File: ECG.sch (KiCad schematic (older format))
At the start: 41 parts, among them J1 SJ-3566AN, J2 Conn_01x03, U1 ADR4525, U2 LTC3531, U7 ADS1015IDGS

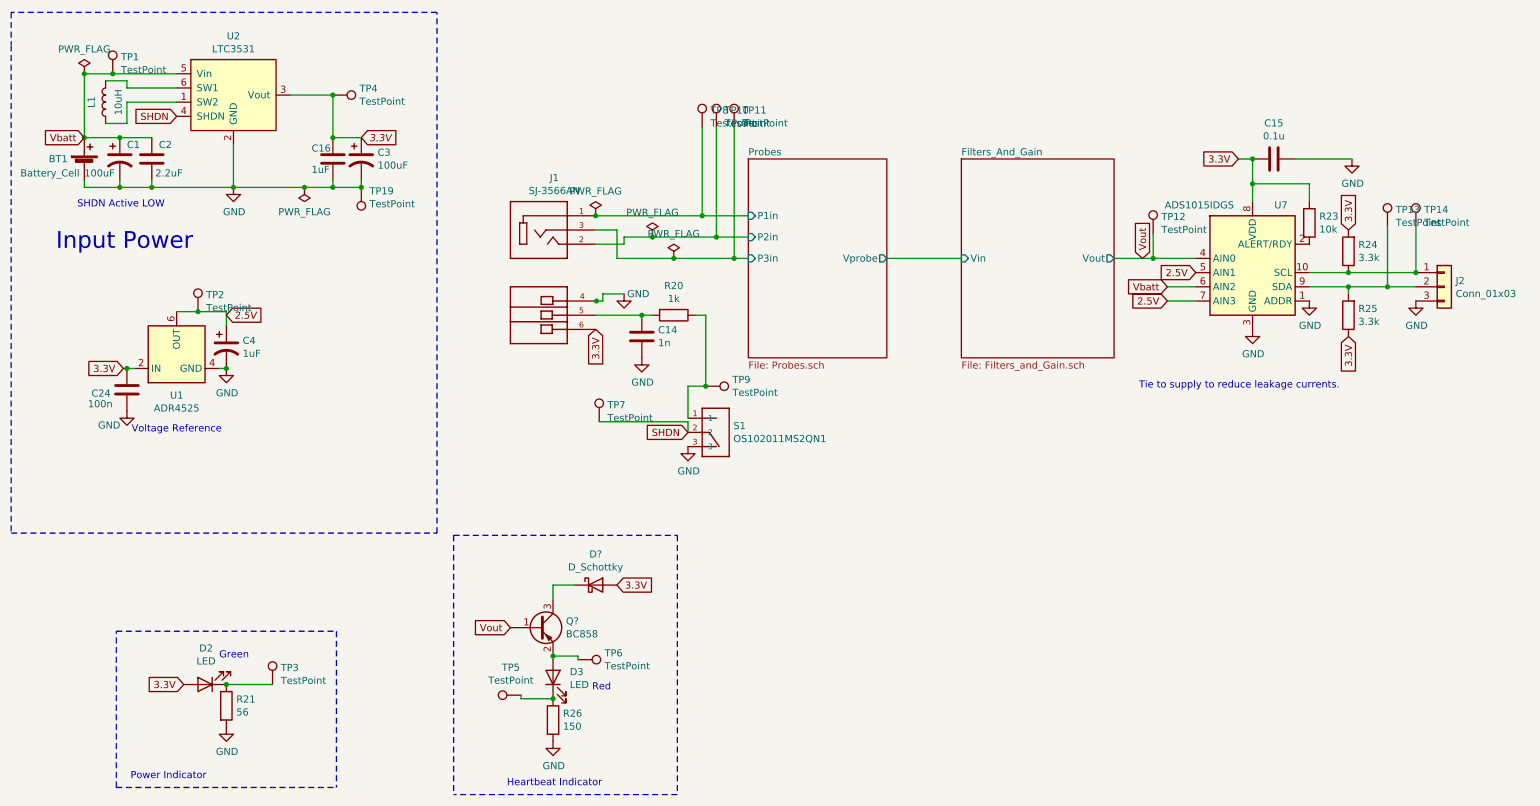
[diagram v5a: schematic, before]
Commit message: #6 - Add bluetooth module to board.
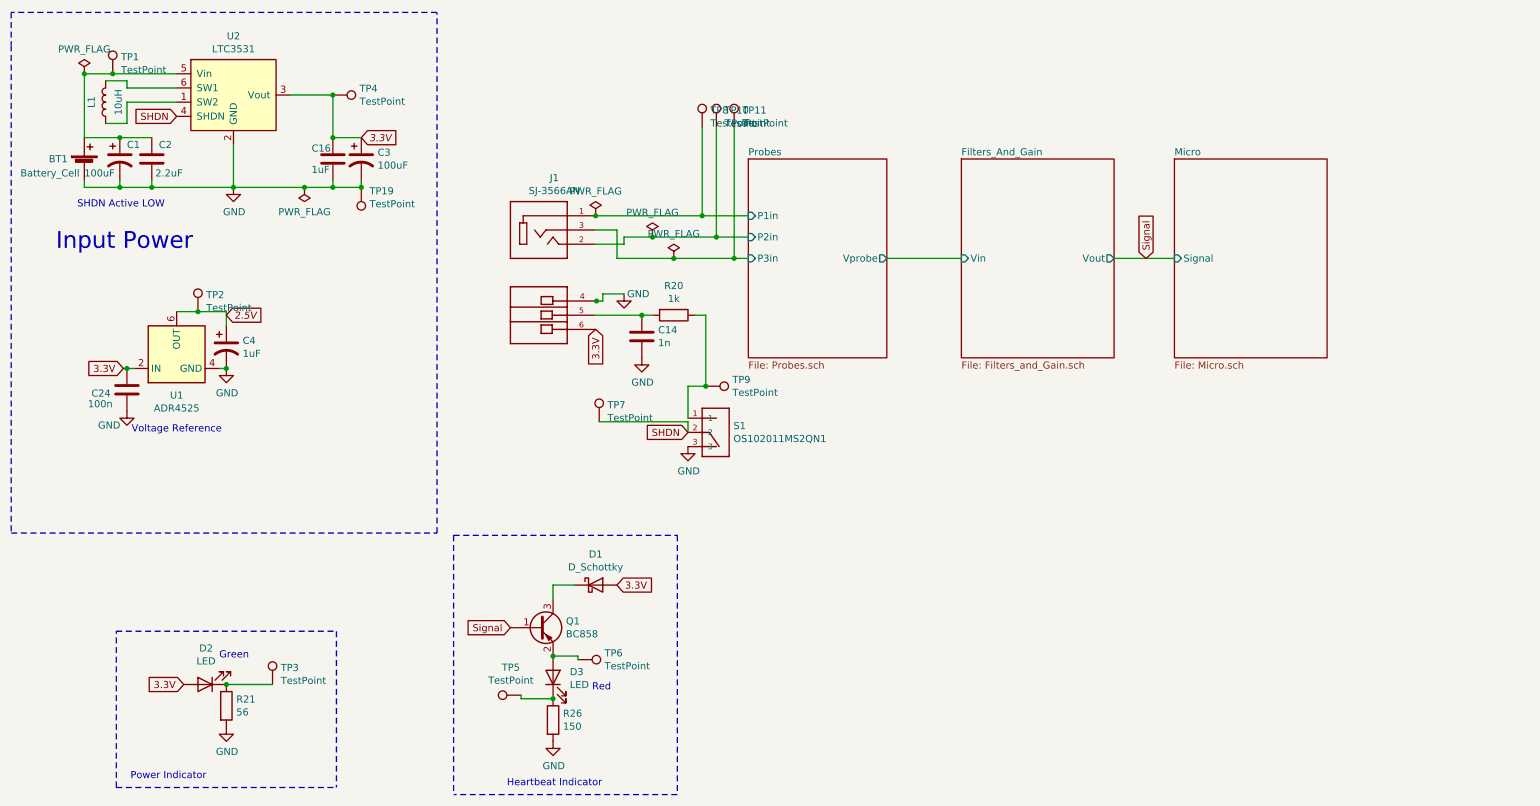
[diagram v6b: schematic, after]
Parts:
- removed C15: 0.1u, Capacitor_SMD:C_0805_2012Metric_Pad1.18x1.45mm_HandSolder, symbol Device:C
- removed J2: Conn_01x03, Connector_PinHeader_2.00mm:PinHeader_1x03_P2.00mm_Vertical, symbol Connector_Generic:Conn_01x03
- removed R23: 10k, Resistor_SMD:R_0805_2012Metric_Pad1.20x1.40mm_HandSolder, symbol Device:R
- removed R24, R25: 3.3k, Resistor_SMD:R_0805_2012Metric_Pad1.20x1.40mm_HandSolder, symbol Device:R
- removed TP12, TP13, TP14: TestPoint, TestPoint:TestPoint_Pad_D2.0mm, symbol Connector:TestPoint
- removed U7: ADS1015IDGS, Package_SO:TSSOP-10_3x3mm_P0.5mm, symbol Analog_ADC:ADS1015IDGS
- gave numbers to parts that had none: 2
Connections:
- net Vbatt: no longer names the net of BT1.1 (+), C1.1, C2.1, TP1.1, U2.5 (Vin)
- net Vout renamed Signal
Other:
- note removed: "Tie to supply to reduce leakage currents."
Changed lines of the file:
@@
 $Descr A4 11693 8268
 encoding utf-8
-Sheet 1 3
+Sheet 1 4
 Title "Power"
 Date ""
@@
 Text Notes 1725 7175 0    50   ~ 0
 Power Indicator
-$Comp
-L Analog_ADC:ADS1015IDGS U7
-U 1 1 5FBE58F1
-P 9625 3600
-F 0 "U7" H 9825 4075 50  0000 C CNN
-F 1 "ADS1015IDGS" H 9250 4075 50  0000 C CNN
-F 2 "Package_SO:TSSOP-10_3x3mm_P0.5mm" H 9625 3100 50  0001 C CNN
-F 3 "http://www.ti.com/lit/ds/symlink/ads1015.pdf" H 9575 2700 50  0001 C CNN
-	1    9625 3600
-	1    0    0    -1
-$EndComp
-$Comp
-L power:GND #PWR015
-U 1 1 5FBF14F2
-P 9625 4000
-F 0 "#PWR015" H 9625 3750 50  0001 C CNN
-F 1 "GND" H 9630 3827 50  0000 C CNN
-F 2 "" H 9625 4000 50  0001 C CNN
-F 3 "" H 9625 4000 50  0001 C CNN
-	1    9625 4000
-	1    0    0    -1
-$EndComp
-Text GLabel 9525 2800 0    50   Input ~ 0
-3.3V
-$Comp
-L Device:C C15
-U 1 1 5FBF2959
-P 9775 2800
-F 0 "C15" V 9523 2800 50  0000 C CNN
-F 1 "0.1u" V 9614 2800 50  0000 C CNN
-F 2 "Capacitor_SMD:C_0805_2012Metric_Pad1.18x1.45mm_HandSolder" H 9813 2650 50  0001 C CNN
-F 3 "~" H 9775 2800 50  0001 C CNN
-	1    9775 2800
-	0    1    1    0
-$EndComp
-Wire Wire Line
-	9625 2800 9625 2975
-Wire Wire Line
-	9625 2800 9525 2800
-Connection ~ 9625 2800
-$Comp
-L power:GND #PWR017
-U 1 1 5FBFA432
-P 10325 2800
-F 0 "#PWR017" H 10325 2550 50  0001 C CNN
-F 1 "GND" H 10330 2627 50  0000 C CNN
-F 2 "" H 10325 2800 50  0001 C CNN
-F 3 "" H 10325 2800 50  0001 C CNN
-	1    10325 2800
-	1    0    0    -1
-$EndComp
-$Comp
-L Device:R R23
-U 1 1 5FC01BDB
-P 10025 3250
-F 0 "R23" H 10095 3296 50  0000 L CNN
-F 1 "10k" H 10095 3205 50  0000 L CNN
-F 2 "Resistor_SMD:R_0805_2012Metric_Pad1.20x1.40mm_HandSolder" V 9955 3250 50  0001 C CNN
-F 3 "~" H 10025 3250 50  0001 C CNN
-	1    10025 3250
-	1    0    0    -1
-$EndComp
-$Comp
-L Device:R R25
-U 1 1 5FC054BC
-P 10300 3900
-F 0 "R25" H 10230 3854 50  0000 R CNN
-F 1 "3.3k" H 10230 3945 50  0000 R CNN
-F 2 "Resistor_SMD:R_0805_2012Metric_Pad1.20x1.40mm_HandSolder" V 10230 3900 50  0001 C CNN
-F 3 "~" H 10300 3900 50  0001 C CNN
-	1    10300 3900
-	-1   0    0    1
-$EndComp
-$Comp
-L Device:R R24
-U 1 1 5FC0648F
-P 10300 3450
-F 0 "R24" H 10230 3404 50  0000 R CNN
-F 1 "3.3k" H 10230 3495 50  0000 R CNN
-F 2 "Resistor_SMD:R_0805_2012Metric_Pad1.20x1.40mm_HandSolder" V 10230 3450 50  0001 C CNN
-F 3 "~" H 10300 3450 50  0001 C CNN
-	1    10300 3450
-	-1   0    0    1
-$EndComp
-Wire Wire Line
-	10025 3700 10300 3700
-Wire Wire Line
-	10300 3700 10300 3750
-Wire Wire Line
-	10300 3700 10575 3700
-Connection ~ 10300 3700
-Wire Wire Line
-	10300 3600 10025 3600
-Connection ~ 10300 3600
-Text GLabel 10300 3300 1    50   Input ~ 0
-3.3V
-Text GLabel 10300 4050 3    50   Input ~ 0
-3.3V
-$Comp
-L power:GND #PWR016
-U 1 1 5FC0ADCB
-P 10025 3800
-F 0 "#PWR016" H 10025 3550 50  0001 C CNN
-F 1 "GND" H 10030 3627 50  0000 C CNN
-F 2 "" H 10025 3800 50  0001 C CNN
-F 3 "" H 10025 3800 50  0001 C CNN
-	1    10025 3800
-	1    0    0    -1
-$EndComp
-Wire Wire Line
-	8650 3500 8925 3500
-Text GLabel 9225 3600 0    50   Input ~ 0
-2.5V
-Wire Wire Line
-	9225 3700 9025 3700
-Wire Wire Line
-	9225 3800 9025 3800
-Text Notes 8825 4425 0    50   ~ 0
-Tie to supply to reduce leakage currents.
-Wire Wire Line
-	9925 2800 10325 2800
-Wire Wire Line
-	10025 3100 10025 2975
-Wire Wire Line
-	10025 2975 9625 2975
-Connection ~ 9625 2975
-Wire Wire Line
-	9625 2975 9625 3100
 Wire Wire Line
 	7050 3500 7575 3500
 Text Notes 2350 6325 0    50   ~ 0
 Green\n
-Text GLabel 8850 3500 1    50   Input ~ 0
-Vout
-Text GLabel 4400 6100 0    50   Input ~ 0
-Vout
 Text GLabel 5150 5800 2    50   Input ~ 0
 3.3V
@@
 Wire Wire Line
 	5650 4725 5650 4650
-$Comp
-L Connector:TestPoint TP14
-U 1 1 5FC95E35
-P 10775 3275
-F 0 "TP14" H 10833 3393 50  0000 L CNN
-F 1 "TestPoint" H 10833 3302 50  0000 L CNN
-F 2 "TestPoint:TestPoint_Pad_D2.0mm" H 10975 3275 50  0001 C CNN
-F 3 "~" H 10975 3275 50  0001 C CNN
-	1    10775 3275
-	1    0    0    -1
-$EndComp
-$Comp
-L Connector:TestPoint TP13
-U 1 1 5FC9653A
-P 10575 3275
-F 0 "TP13" H 10633 3393 50  0000 L CNN
-F 1 "TestPoint" H 10633 3302 50  0000 L CNN
-F 2 "TestPoint:TestPoint_Pad_D2.0mm" H 10775 3275 50  0001 C CNN
-F 3 "~" H 10775 3275 50  0001 C CNN
-	1    10575 3275
-	1    0    0    -1
-$EndComp
-Wire Wire Line
-	10775 3275 10775 3600
-$Comp
-L Connector:TestPoint TP12
-U 1 1 5FCA6AF9
-P 8925 3325
-F 0 "TP12" H 8983 3443 50  0000 L CNN
-F 1 "TestPoint" H 8983 3352 50  0000 L CNN
-F 2 "TestPoint:TestPoint_Pad_D2.0mm" H 9125 3325 50  0001 C CNN
-F 3 "~" H 9125 3325 50  0001 C CNN
-	1    8925 3325
-	1    0    0    -1
-$EndComp
-Wire Wire Line
-	8925 3325 8925 3500
-Connection ~ 8925 3500
-Wire Wire Line
-	8925 3500 9225 3500
 Wire Wire Line
 	4700 6300 4875 6300
@@
 	1    0    0    -1
 $EndComp
-Text GLabel 9025 3700 0    50   Input ~ 0
-Vbatt
-Text GLabel 9025 3800 0    50   Input ~ 0
-2.5V
 Text GLabel 2100 6500 0    50   Input ~ 0
 3.3V
-$Comp
-L Connector_Generic:Conn_01x03 J2
-U 1 1 5FCF854F
-P 10975 3700
-F 0 "J2" H 11055 3742 50  0000 L CNN
-F 1 "Conn_01x03" H 11055 3651 50  0000 L CNN
-F 2 "Connector_PinHeader_2.00mm:PinHeader_1x03_P2.00mm_Vertical" H 10975 3700 50  0001 C CNN
-F 3 "~" H 10975 3700 50  0001 C CNN
-	1    10975 3700
-	1    0    0    -1
-$EndComp
-Connection ~ 10775 3600
-$Comp
-L power:GND #PWR020
-U 1 1 5FCF90A6
-P 10775 3800
-F 0 "#PWR020" H 10775 3550 50  0001 C CNN
-F 1 "GND" H 10780 3627 50  0000 C CNN
-F 2 "" H 10775 3800 50  0001 C CNN
-F 3 "" H 10775 3800 50  0001 C CNN
-	1    10775 3800
-	1    0    0    -1
-$EndComp
 Wire Wire Line
 	6075 3200 5750 3200
@@
 	6075 3500 5975 3500
 Connection ~ 5975 3500
-Connection ~ 10575 3700
-Wire Wire Line
-	10575 3700 10775 3700
-Wire Wire Line
-	10300 3600 10775 3600
-Wire Wire Line
-	10575 3275 10575 3700
 $Comp
 L Device:C C2
@@
 Wire Wire Line
 	1400 2200 1600 2200
-Connection ~ 1400 2650
 Wire Wire Line
 	2050 2400 1700 2400
@@
 Connection ~ 3150 2650
 Connection ~ 3150 2350
-Text GLabel 1400 2650 0    50   Input ~ 0
-Vbatt
 Wire Notes Line
 	1625 6125 3175 6125
@@
 	1625 7225 3175 7225
 $Comp
-L Transistor_BJT:BC858 Q?
+L Transistor_BJT:BC858 Q1
 U 1 1 5FDAC112
 P 4600 6100
-F 0 "Q?" H 4791 6146 50  0000 L CNN
+F 0 "Q1" H 4791 6146 50  0000 L CNN
 F 1 "BC858" H 4791 6055 50  0000 L CNN
 F 2 "Package_TO_SOT_SMD:SOT-23" H 4800 6025 50  0001 L CIN
@@
 	5575 5450 5575 7275
 $Comp
-L Device:D_Schottky D?
+L Device:D_Schottky D1
 U 1 1 5FDC078D
 P 5000 5800
-F 0 "D?" H 5000 6017 50  0000 C CNN
+F 0 "D1" H 5000 6017 50  0000 C CNN
 F 1 "D_Schottky" H 5000 5926 50  0000 C CNN
 F 2 "Diode_SMD:D_0603_1608Metric_Pad1.05x0.95mm_HandSolder" H 5000 5800 50  0001 C CNN
@@
 F3 "Vin" I L 7575 3500 50
 $EndSheet
+$Sheet
+S 9075 2800 1075 1400
+U 5FDD9C20
+F0 "Micro" 50
+F1 "Micro.sch" 50
+F2 "Signal" I L 9075 3500 50
+$EndSheet
+Wire Wire Line
+	9075 3500 8650 3500
+Text GLabel 8875 3500 1    50   Input ~ 0
+Signal
+Text GLabel 4400 6100 0    50   Input ~ 0
+Signal
 $EndSCHEMATC

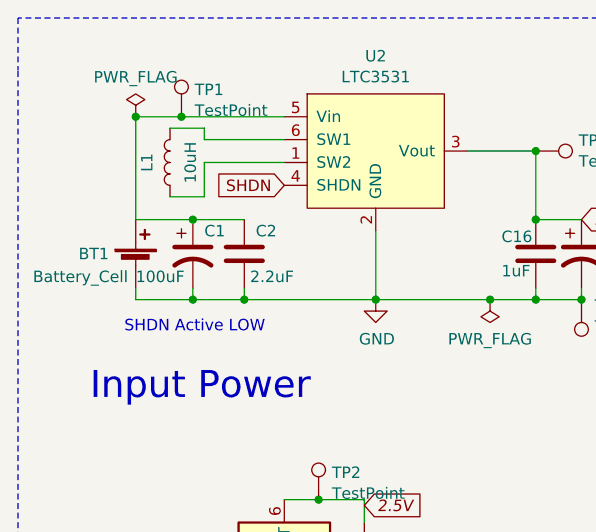
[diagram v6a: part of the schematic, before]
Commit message: #6 #14 - Add bluetooth and flash header to board
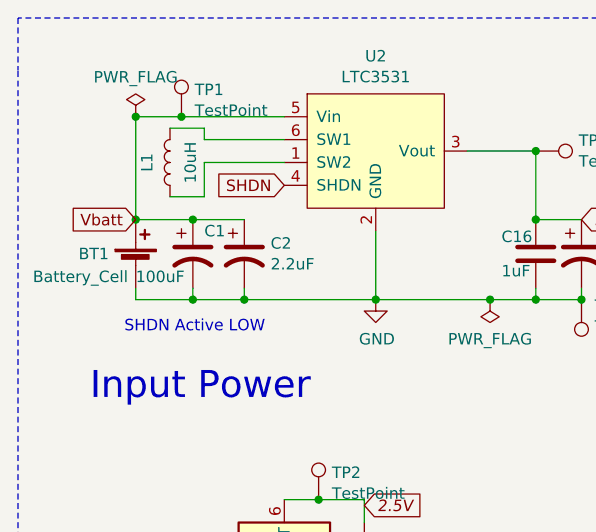
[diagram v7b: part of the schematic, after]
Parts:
- removed C2: 2.2uF, symbol Device:C
- added C2: 2.2uF, Capacitor_SMD:CP_Elec_4x5.7, symbol Device:CP1
- C16: footprint (none) -> Capacitor_SMD:CP_Elec_4x5.3
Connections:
- net GND: now also C2.2
- net Vbatt: now reaches BT1.1 (+), C1.1, TP1.1, U2.5 (Vin)
- net Vbatt: now also C2.1
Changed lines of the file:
@@
 	6075 3500 5975 3500
 Connection ~ 5975 3500
-$Comp
-L Device:C C2
-U 1 1 5FD5C986
-P 1875 2800
-F 0 "C2" H 1925 2900 50  0000 L CNN
-F 1 "2.2uF" H 1900 2700 50  0000 L CNN
-F 2 "" H 1913 2650 50  0001 C CNN
-F 3 "~" H 1875 2800 50  0001 C CNN
-	1    1875 2800
-	1    0    0    -1
-$EndComp
 Connection ~ 1650 2650
 Wire Wire Line
@@
 F 0 "C16" H 3000 2875 50  0000 L CNN
 F 1 "1uF" H 3000 2725 50  0000 L CNN
-F 2 "" H 3188 2650 50  0001 C CNN
+F 2 "Capacitor_SMD:CP_Elec_4x5.3" H 3188 2650 50  0001 C CNN
 F 3 "~" H 3150 2800 50  0001 C CNN
 	1    3150 2800
@@
 Text GLabel 4400 6100 0    50   Input ~ 0
 Signal
+Text GLabel 1400 2650 0    50   Input ~ 0
+Vbatt
+Connection ~ 1400 2650
+$Comp
+L Device:CP1 C2
+U 1 1 5FE0A857
+P 1875 2800
+F 0 "C2" H 1990 2846 50  0000 L CNN
+F 1 "2.2uF" H 1990 2755 50  0000 L CNN
+F 2 "Capacitor_SMD:CP_Elec_4x5.7" H 1875 2800 50  0001 C CNN
+F 3 "~" H 1875 2800 50  0001 C CNN
+	1    1875 2800
+	1    0    0    -1
+$EndComp
 $EndSCHEMATC

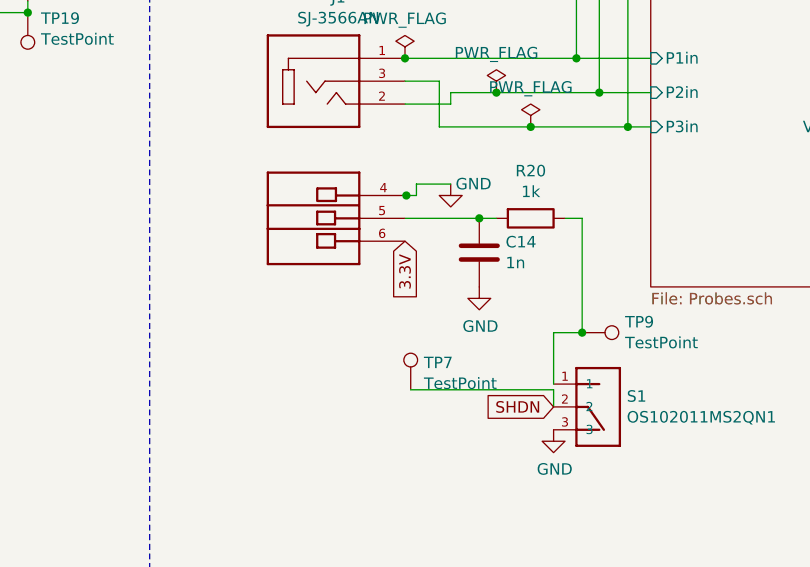
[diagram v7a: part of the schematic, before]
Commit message: #21 - Hook up switch to battery line
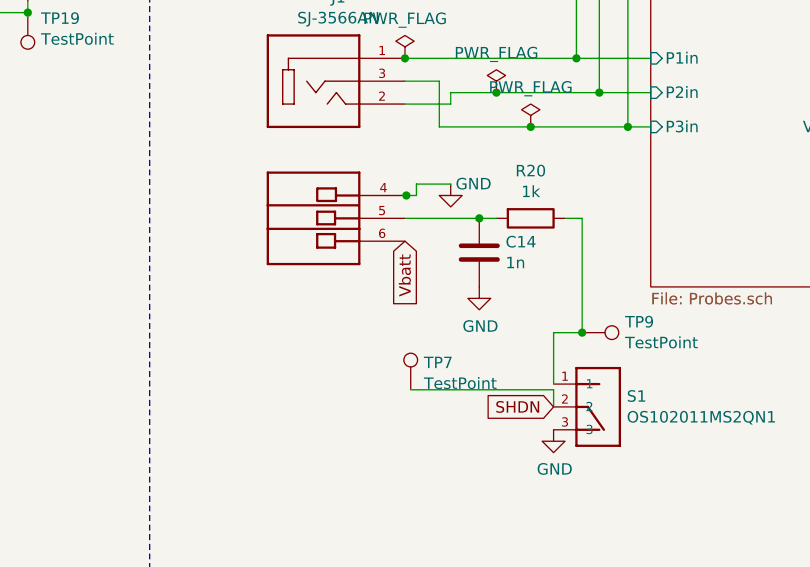
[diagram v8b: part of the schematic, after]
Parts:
- C3: footprint Capacitor_SMD:CP_Elec_5x5.3 -> Capacitor_SMD:CP_Elec_6.3x5.3
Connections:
- net 3.3V: no longer J1.6
- net Vbatt: now also J1.6
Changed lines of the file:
@@
 F 0 "C3" H 3465 2846 50  0000 L CNN
 F 1 "100uF" H 3465 2755 50  0000 L CNN
-F 2 "Capacitor_SMD:CP_Elec_5x5.3" H 3350 2800 50  0001 C CNN
+F 2 "Capacitor_SMD:CP_Elec_6.3x5.3" H 3350 2800 50  0001 C CNN
 F 3 "~" H 3350 2800 50  0001 C CNN
 	1    3350 2800
@@
 	1    0    0    -1
 $EndComp
-Text GLabel 5000 4000 3    50   Input ~ 0
-3.3V
 Wire Wire Line
 	1400 2650 1650 2650
@@
 	1    0    0    -1
 $EndComp
+Text GLabel 5000 4000 3    50   Input ~ 0
+Vbatt
 $EndSCHEMATC
